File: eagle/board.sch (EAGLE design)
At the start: 23 parts, among them X1 2.1MMJACKTHM, X10 10p-2.0, X11 MOUNTING_HOLE3.2MM_SILK, X12 MOUNTING_HOLE3.2MM_SILK, X13 MOUNTING_HOLE3.2MM_SILK, X14 MOUNTING_HOLE3.2MM_SILK, X2 2p-2.0, X3 5p-2.54, X4 8p-2.54, X5 14p-2.54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

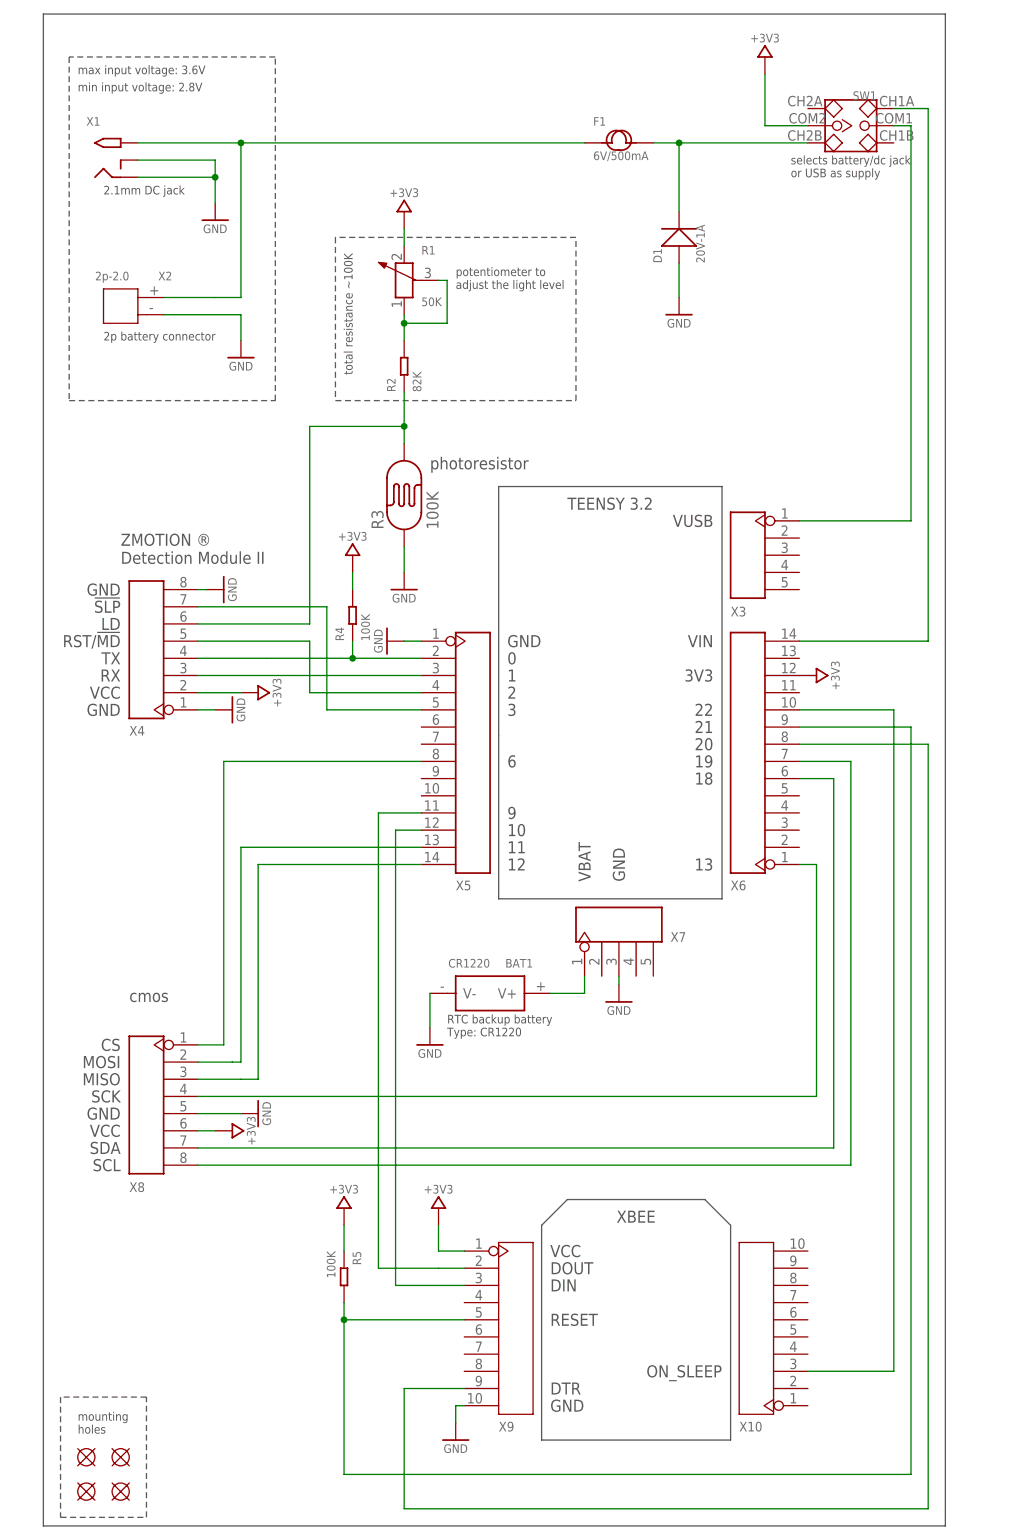
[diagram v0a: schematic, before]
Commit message: new slide switch new capacitors
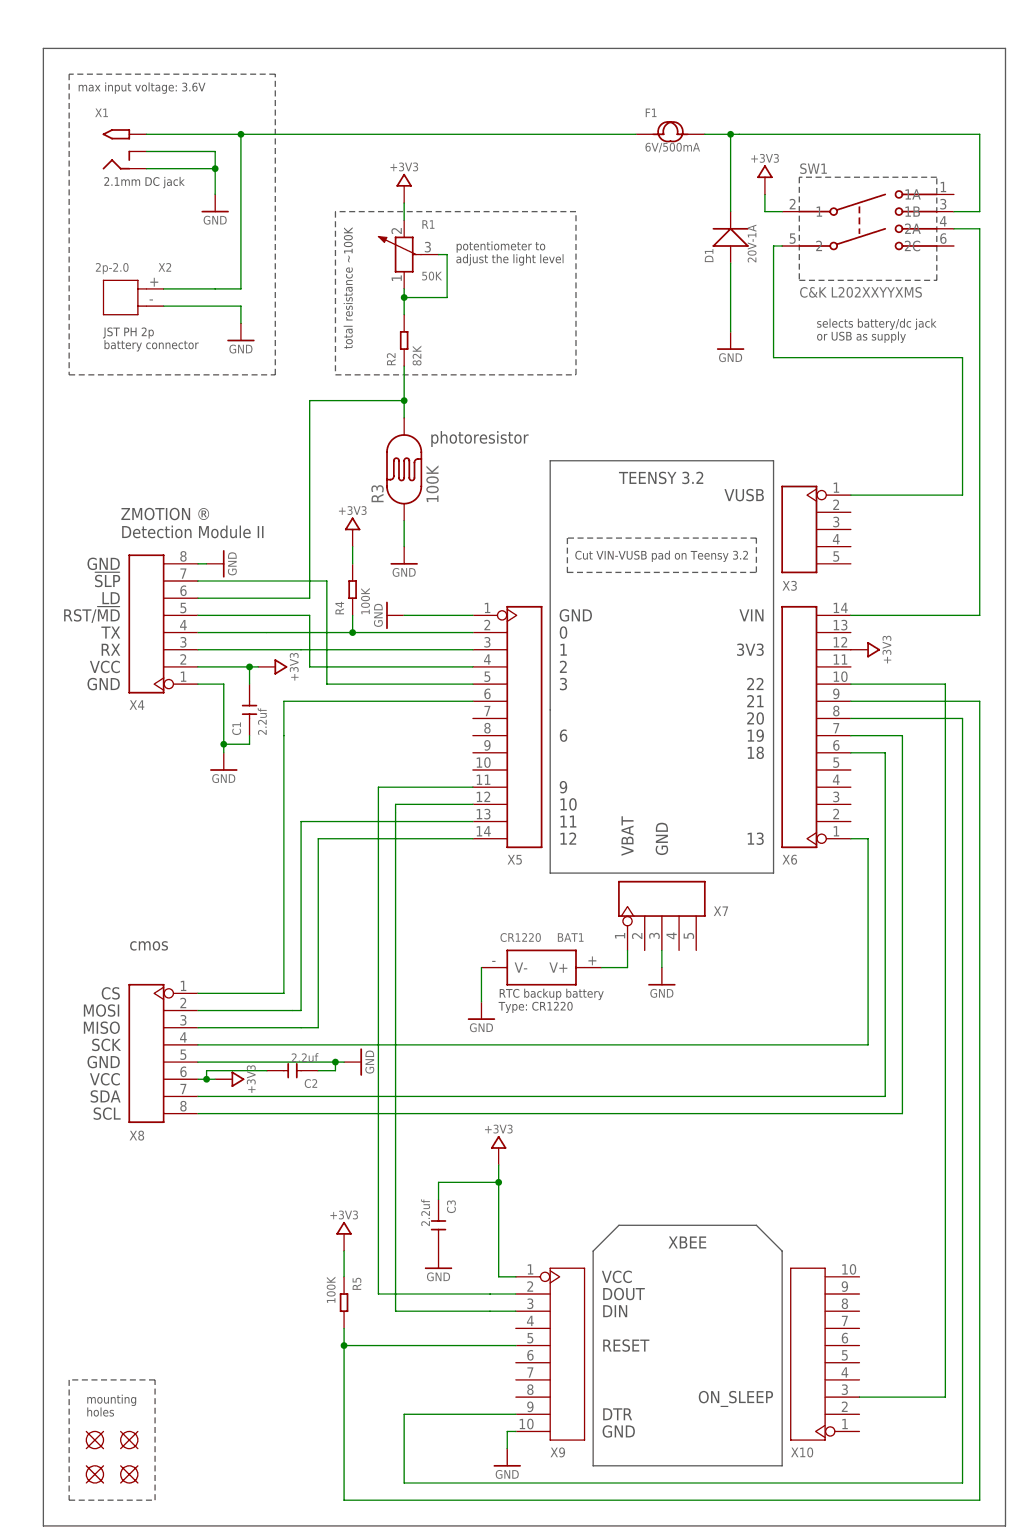
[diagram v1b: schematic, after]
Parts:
- removed X11, X12, X13, X14: MOUNTING_HOLE3.2MM_SILK, teensybee:MOUNTING_HOLE3.2MM_SILK
- added C1, C2, C3: 2.2uf, Seeed-OPL-Capacitor:CERAMIC-2.2UF-25V-10%-X7R(0805)
- added MNT1, MNT2, MNT3, MNT4: MOUNTING_HOLE3.2MM_SILK, teensybee:MOUNTING_HOLE3.2MM_SILK
- SW1: value (none) -> C&K L202XXYYXMS; device teensybee:DIP-TOGGLE-SWITCH-2CH-(2X3P-2.54) -> teensybee:DPDTL202XXYYXMS
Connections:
- net +3V3: now also C1.2, C2.2, C3.1, SW1.1; no longer SW1.COM2
- net GND: now also C1.1, C2.1, C3.2
- net N$13: now also X5.6; no longer X5.8
- net N$18: now also SW1.2A; no longer SW1.CH1A
- net N$19: now also SW1.2; no longer SW1.COM1
- net N$20: now also SW1.1B; no longer SW1.CH2B
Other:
- note added: "Cut VIN-VUSB pad on Teensy 3.2"
- note added: "JST PH 2p battery connector"
- note removed: "2p battery connector"
- note removed: "min input voltage: 2.8V"
- moved on the sheet: BAT1, D1, F1, R1, R2, R3, R4, R5, X1, X10, X2, X3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

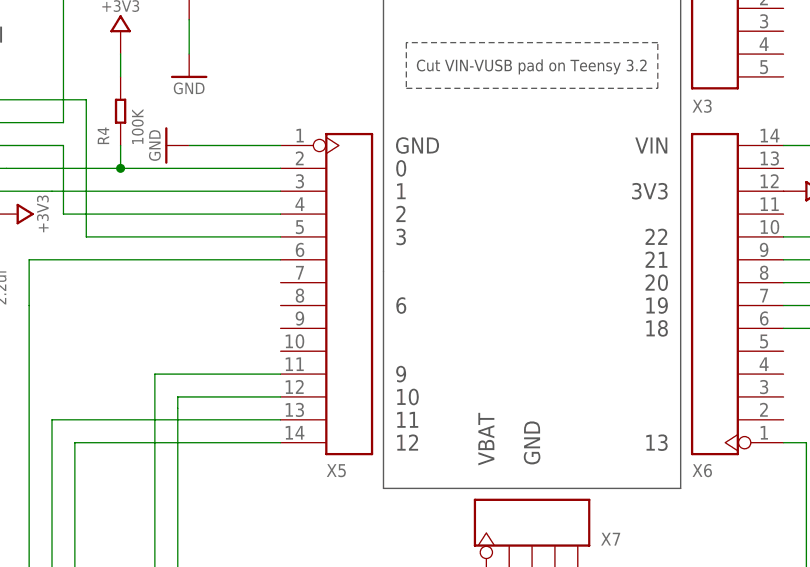
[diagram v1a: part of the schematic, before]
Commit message: fix silkscreen for pin 4
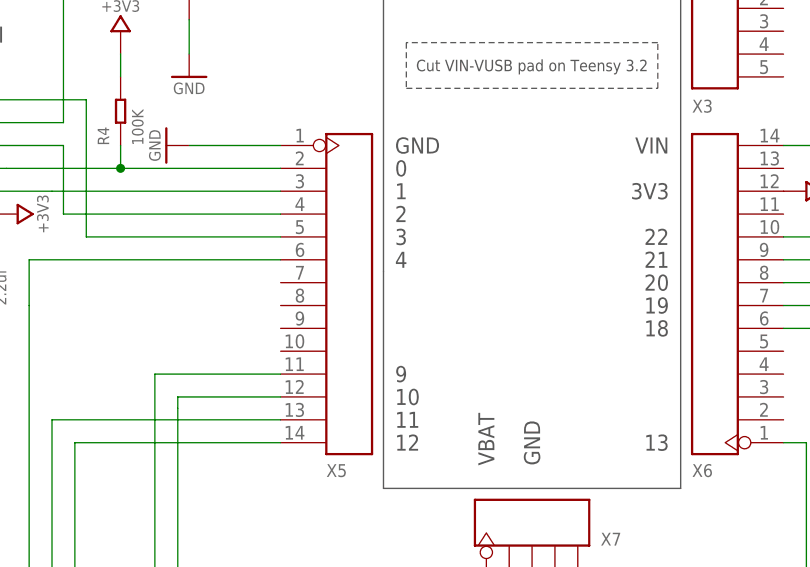
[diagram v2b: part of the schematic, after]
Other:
- note added: "4"
- note removed: "6"
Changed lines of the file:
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@@
 <grid distance="0.05" unitdist="inch" unit="inch" style="lines" multiple="1" display="yes" altdistance="0.01" altunitdist="inch" altunit="inch"/>
 <layers>
-<layer number="1" name="Top" color="4" fill="1" visible="yes" active="no"/>
-<layer number="16" name="Bottom" color="1" fill="1" visible="yes" active="no"/>
-<layer number="17" name="Pads" color="2" fill="1" visible="yes" active="no"/>
-<layer number="18" name="Vias" color="2" fill="1" visible="yes" active="no"/>
-<layer number="19" name="Unrouted" color="6" fill="1" visible="yes" active="no"/>
-<layer number="20" name="Dimension" color="15" fill="1" visible="yes" active="no"/>
-<layer number="21" name="tPlace" color="7" fill="1" visible="yes" active="no"/>
-<layer number="22" name="bPlace" color="7" fill="1" visible="yes" active="no"/>
-<layer number="23" name="tOrigins" color="15" fill="1" visible="yes" active="no"/>
-<layer number="24" name="bOrigins" color="15" fill="1" visible="yes" active="no"/>
-<layer number="25" name="tNames" color="7" fill="1" visible="yes" active="no"/>
-<layer number="26" name="bNames" color="7" fill="1" visible="yes" active="no"/>
-<layer number="27" name="tValues" color="7" fill="1" visible="yes" active="no"/>
-<layer number="28" name="bValues" color="7" fill="1" visible="yes" active="no"/>
+<layer number="1" name="Top" color="4" fill="1" visible="no" active="no"/>
+<layer number="16" name="Bottom" color="1" fill="1" visible="no" active="no"/>
+<layer number="17" name="Pads" color="2" fill="1" visible="no" active="no"/>
+<layer number="18" name="Vias" color="2" fill="1" visible="no" active="no"/>
+<layer number="19" name="Unrouted" color="6" fill="1" visible="no" active="no"/>
+<layer number="20" name="Dimension" color="15" fill="1" visible="no" active="no"/>
+<layer number="21" name="tPlace" color="7" fill="1" visible="no" active="no"/>
+<layer number="22" name="bPlace" color="7" fill="1" visible="no" active="no"/>
+<layer number="23" name="tOrigins" color="15" fill="1" visible="no" active="no"/>
+<layer number="24" name="bOrigins" color="15" fill="1" visible="no" active="no"/>
+<layer number="25" name="tNames" color="7" fill="1" visible="no" active="no"/>
+<layer number="26" name="bNames" color="7" fill="1" visible="no" active="no"/>
+<layer number="27" name="tValues" color="7" fill="1" visible="no" active="no"/>
+<layer number="28" name="bValues" color="7" fill="1" visible="no" active="no"/>
 <layer number="29" name="tStop" color="7" fill="3" visible="no" active="no"/>
 <layer number="30" name="bStop" color="7" fill="6" visible="no" active="no"/>
@@
 <layer number="35" name="tGlue" color="7" fill="4" visible="no" active="no"/>
 <layer number="36" name="bGlue" color="7" fill="5" visible="no" active="no"/>
-<layer number="37" name="tTest" color="7" fill="1" visible="yes" active="no"/>
-<layer number="38" name="bTest" color="7" fill="1" visible="yes" active="no"/>
+<layer number="37" name="tTest" color="7" fill="1" visible="no" active="no"/>
+<layer number="38" name="bTest" color="7" fill="1" visible="no" active="no"/>
 <layer number="39" name="tKeepout" color="4" fill="11" visible="no" active="no"/>
 <layer number="40" name="bKeepout" color="1" fill="11" visible="no" active="no"/>
@@
 <layer number="44" name="Drills" color="7" fill="1" visible="no" active="no"/>
 <layer number="45" name="Holes" color="7" fill="1" visible="no" active="no"/>
-<layer number="46" name="Milling" color="3" fill="1" visible="yes" active="no"/>
-<layer number="47" name="Measures" color="7" fill="1" visible="yes" active="no"/>
-<layer number="48" name="Document" color="7" fill="1" visible="yes" active="no"/>
-<layer number="49" name="Reference" color="7" fill="1" visible="yes" active="no"/>
-<layer number="50" name="dxf" color="7" fill="1" visible="yes" active="no"/>
-<layer number="51" name="tDocu" color="14" fill="1" visible="yes" active="no"/>
-<layer number="52" name="bDocu" color="7" fill="1" visible="yes" active="no"/>
-<layer number="53" name="tGND_GNDA" color="7" fill="9" visible="yes" active="no"/>
-<layer number="54" name="bGND_GNDA" color="1" fill="9" visible="yes" active="no"/>
-<layer number="56" name="wert" color="7" fill="1" visible="yes" active="no"/>
-<layer number="57" name="tCAD" color="7" fill="1" visible="yes" active="no"/>
+<layer number="46" name="Milling" color="3" fill="1" visible="no" active="no"/>
+<layer number="47" name="Measures" color="7" fill="1" visible="no" active="no"/>
+<layer number="48" name="Document" color="7" fill="1" visible="no" active="no"/>
+<layer number="49" name="Reference" color="7" fill="1" visible="no" active="no"/>
+<layer number="50" name="dxf" color="7" fill="1" visible="no" active="no"/>
+<layer number="51" name="tDocu" color="14" fill="1" visible="no" active="no"/>
+<layer number="52" name="bDocu" color="7" fill="1" visible="no" active="no"/>
+<layer number="53" name="tGND_GNDA" color="7" fill="9" visible="no" active="no"/>
+<layer number="54" name="bGND_GNDA" color="1" fill="9" visible="no" active="no"/>
+<layer number="56" name="wert" color="7" fill="1" visible="no" active="no"/>
+<layer number="57" name="tCAD" color="7" fill="1" visible="no" active="no"/>
 <layer number="90" name="Modules" color="5" fill="1" visible="yes" active="yes"/>
 <layer number="91" name="Nets" color="2" fill="1" visible="yes" active="yes"/>
@@
 <text x="76.2" y="127" size="1.778" layer="97" align="center-left">2</text>
 <text x="76.2" y="124.46" size="1.778" layer="97" align="center-left">3</text>
-<text x="76.2" y="116.84" size="1.778" layer="97" align="center-left">6</text>
+<text x="76.2" y="121.92" size="1.778" layer="97" align="center-left">4</text>
 <text x="76.2" y="109.22" size="1.778" layer="97" align="center-left">9</text>
 <text x="76.2" y="106.68" size="1.778" layer="97" align="center-left">10</text>
